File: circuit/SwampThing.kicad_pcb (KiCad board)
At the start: 2 copper layers, 100 x 100 mm, 100 parts, among them J1 USB_B, J2 HOLE, J3 HOLE, J4 HOLE, J5 HOLE, Q1 IRFS52N15DTRLP, Q2 BC547, SW1 reset, SW10 4S LiPo, SW11 3S LiPo, SW2 mute, SW3 HEAD/AD, SW6 next, SW8 pause, SW9 6S LiPo, U1 LM2576T-ADJ, U2 LM1117-5.0, U3 MAX6457, U4 LM1117-3.3, U5 TPA3220, U6 CSR_DBG, U7 CSR8645_MODULE

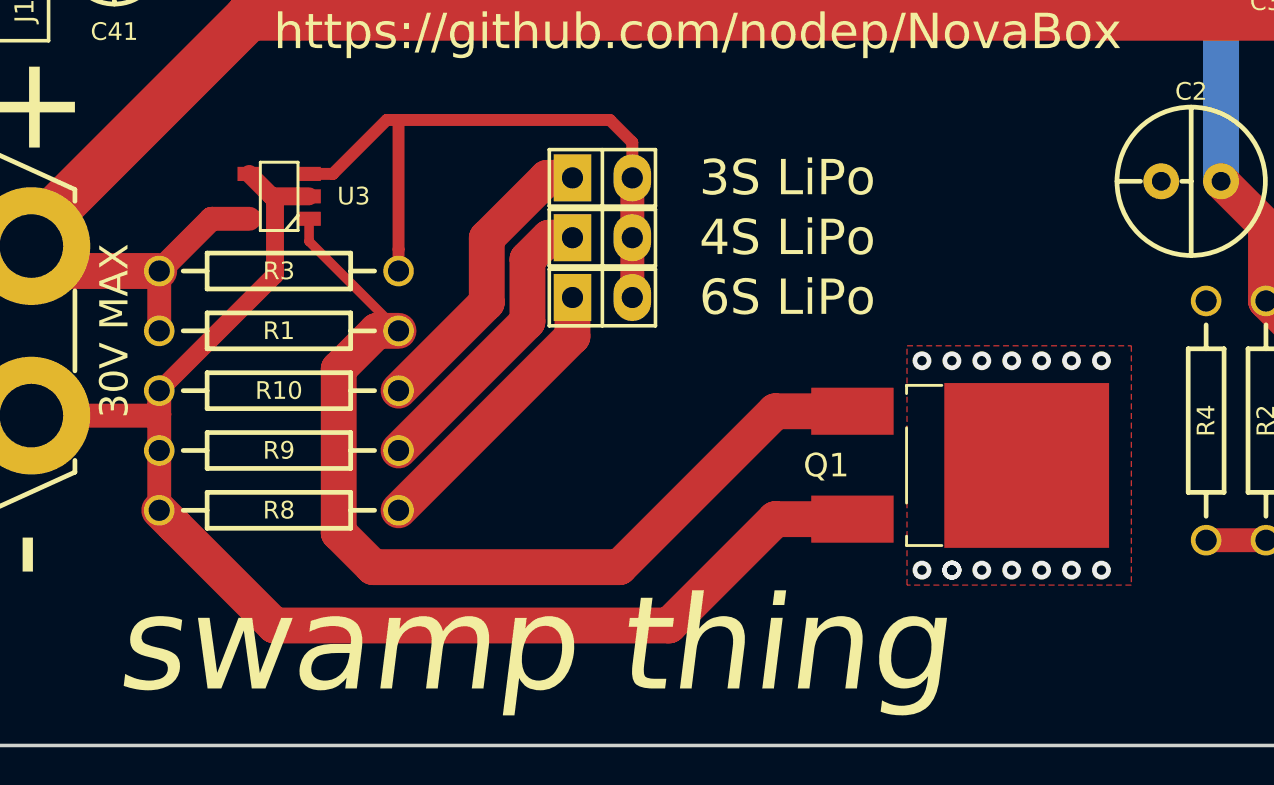
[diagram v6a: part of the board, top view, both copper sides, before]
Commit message: swamp thing assembled! TO-252 changed to TO-263
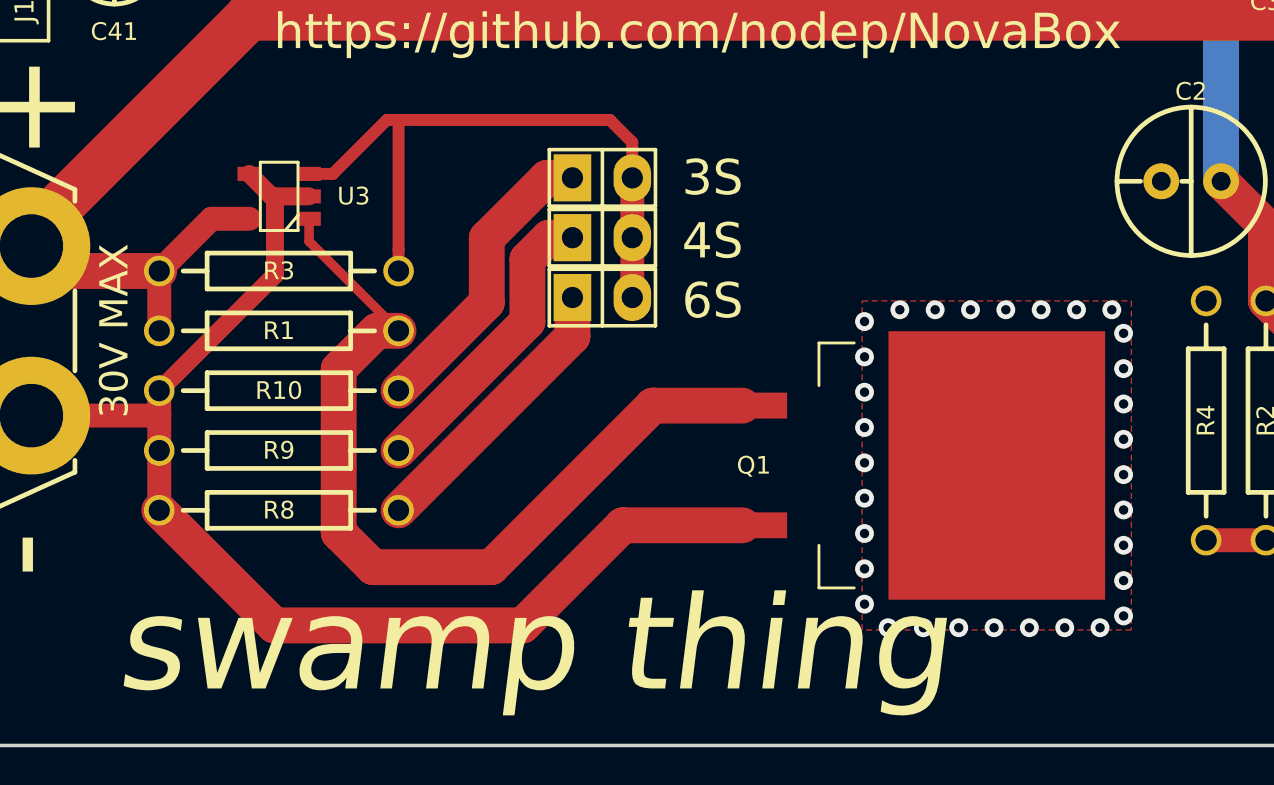
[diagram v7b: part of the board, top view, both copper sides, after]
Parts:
- Q1: footprint NovaBox:TO-252 -> NovaBox:TO-263-2
- SW10: value 4S LiPo -> 4S
- SW11: value 3S LiPo -> 3S
- SW9: value 6S LiPo -> 6S
- moved Q1 3.05 mm to (90.0, 118.1)
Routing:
- net -BATT: track 57.1 -> 52.4 mm
- net /SW_GATE: track 41.7 -> 37.1 mm
- net GND: vias 37 -> 53

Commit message: narrow swamp thingee
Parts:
- removed R6: 100K, NovaBox:R_10MM
- removed REF**: OSHW-Symbol_44.5x40mm_SilkScreen, NovaBox:OSHW-Symbol_44.5x40mm_SilkScreen
- removed REF**: KiCad-Logo2_12mm_SilkScreen, NovaBox:KiCad-Logo2_12mm_SilkScreen
- moved R5 2.54 mm to (87.0, 34.9)
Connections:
- S4 pad 1: Net-(R6-Pad2) -> Net-(R5-Pad2)
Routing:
- net Net-(R6-Pad2): track 8.89 -> 0.00 mm
- net Net-(R5-Pad2): track 8.89 -> 11.4 mm
